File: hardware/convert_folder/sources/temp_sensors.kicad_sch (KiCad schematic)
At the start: 25 parts, among them CN14 TSW-101-05-T-S, IC6 MMBT3904, IC7 MMBT3904, U21 LTC2983CLX#PBF

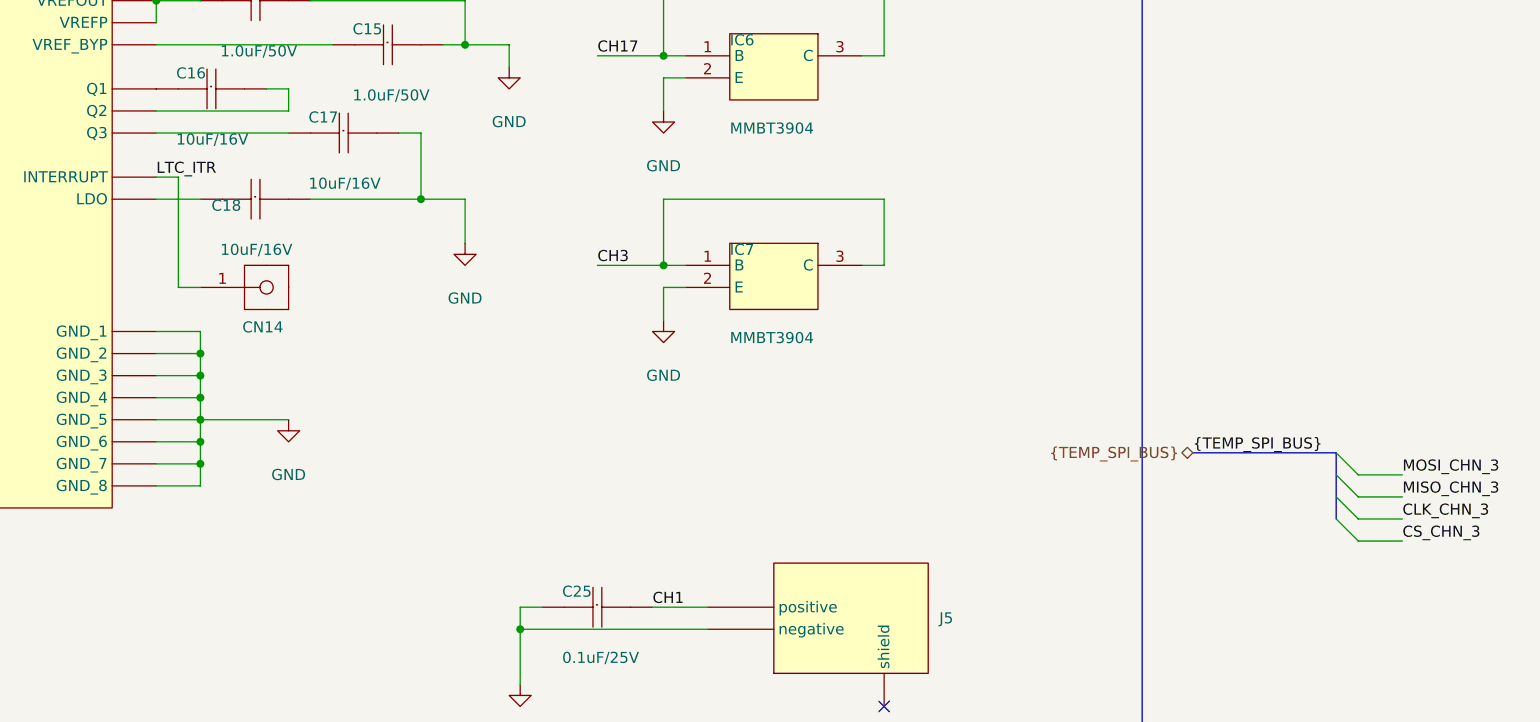
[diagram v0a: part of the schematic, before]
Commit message: fix: add more fixes to the power converters, add resets and other minor corrections
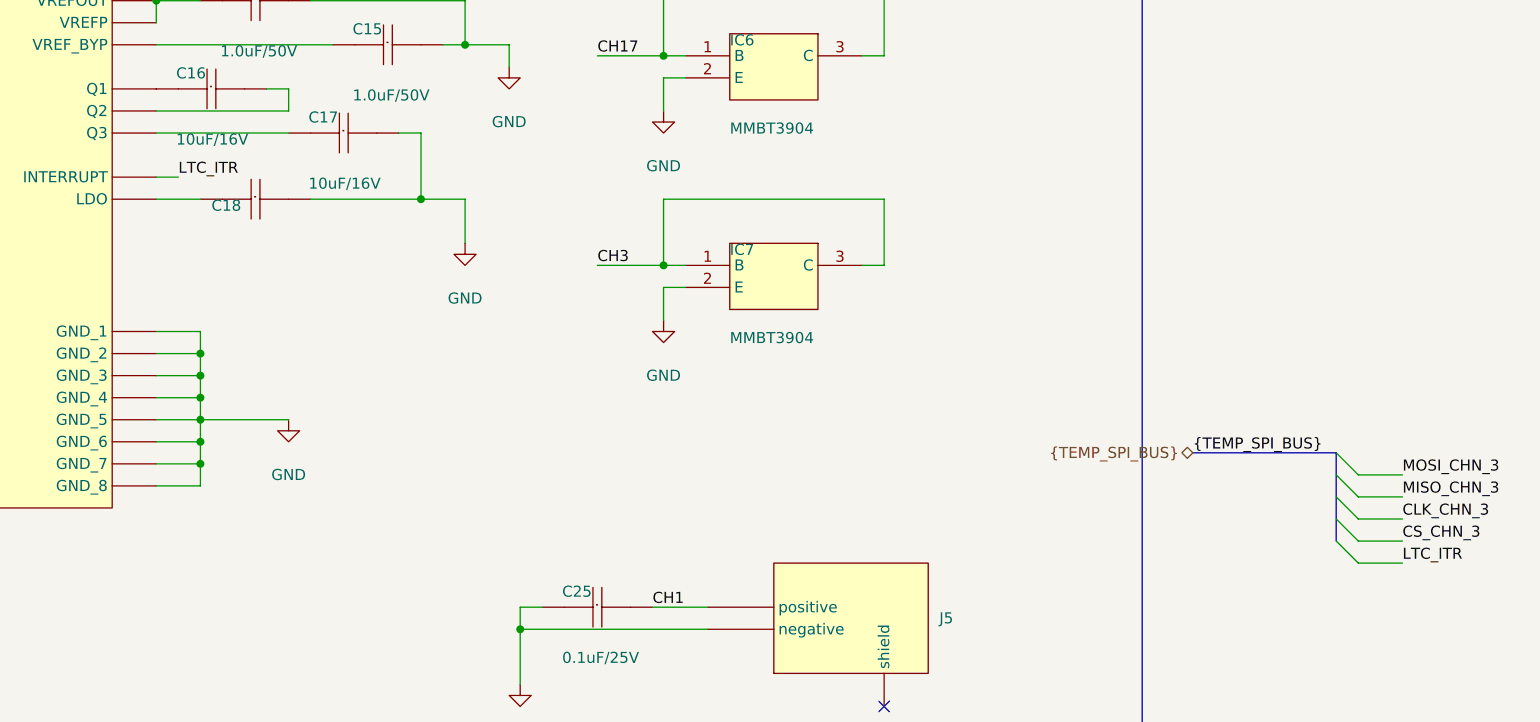
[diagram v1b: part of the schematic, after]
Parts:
- removed CN14: TSW-101-05-T-S, altium_import:PIN BAR 1 2.54mm 180 GRAUS - Hide, symbol altium_import:root_2_TSW-101-05-T-S_flatsat_platform_2.SchLib

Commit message: fix: finish regulators layout and fix many DRCs errors related to clearance
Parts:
- J10, J11, J12, J13, J14, J15, J5, J6: footprint altium_import:PCC-SMP-V-K -> lib:PCC-SMP-V-K-5
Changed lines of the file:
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@@
 	)
 	(symbol
-		(lib_name "root_0_PCC-SMP-V-K_Thermocouple_connector.SchLib_2")
 		(lib_id "altium_import:root_0_PCC-SMP-V-K_Thermocouple_connector.SchLib")
 		(at 289.56 255.27 90)
@@
 			)
 		)
-		(property "Footprint" "altium_import:PCC-SMP-V-K"
+		(property "Footprint" "lib:PCC-SMP-V-K-5"
 			(at 296.926 244.602 0)
 			(effects
@@
 	)
 	(symbol
-		(lib_name "root_0_PCC-SMP-V-K_Thermocouple_connector.SchLib_2")
 		(lib_id "altium_import:root_0_PCC-SMP-V-K_Thermocouple_connector.SchLib")
 		(at 290.83 278.13 90)
@@
 			)
 		)
-		(property "Footprint" "altium_import:PCC-SMP-V-K"
+		(property "Footprint" "lib:PCC-SMP-V-K-5"
 			(at 298.196 267.462 0)
 			(effects
@@
 	)
 	(symbol
-		(lib_name "root_0_PCC-SMP-V-K_Thermocouple_connector.SchLib_2")
 		(lib_id "altium_import:root_0_PCC-SMP-V-K_Thermocouple_connector.SchLib")
 		(at 346.71 278.13 90)
@@
 			)
 		)
-		(property "Footprint" "altium_import:PCC-SMP-V-K"
+		(property "Footprint" "lib:PCC-SMP-V-K-5"
 			(at 354.076 267.462 0)
 			(effects
@@
 	)
 	(symbol
-		(lib_name "root_0_PCC-SMP-V-K_Thermocouple_connector.SchLib_2")
 		(lib_id "altium_import:root_0_PCC-SMP-V-K_Thermocouple_connector.SchLib")
 		(at 232.41 254 90)
@@
 			)
 		)
-		(property "Footprint" "altium_import:PCC-SMP-V-K"
+		(property "Footprint" "lib:PCC-SMP-V-K-5"
 			(at 239.776 243.332 0)
 			(effects
@@
 	)
 	(symbol
-		(lib_name "root_0_PCC-SMP-V-K_Thermocouple_connector.SchLib_2")
 		(lib_id "altium_import:root_0_PCC-SMP-V-K_Thermocouple_connector.SchLib")
 		(at 233.68 278.13 90)
@@
 			)
 		)
-		(property "Footprint" "altium_import:PCC-SMP-V-K"
+		(property "Footprint" "lib:PCC-SMP-V-K-5"
 			(at 241.046 267.462 0)
 			(effects
@@
 	)
 	(symbol
-		(lib_name "root_0_PCC-SMP-V-K_Thermocouple_connector.SchLib_2")
 		(lib_id "altium_import:root_0_PCC-SMP-V-K_Thermocouple_connector.SchLib")
 		(at 345.44 229.87 90)
@@
 			)
 		)
-		(property "Footprint" "altium_import:PCC-SMP-V-K"
+		(property "Footprint" "lib:PCC-SMP-V-K-5"
 			(at 352.806 219.202 0)
 			(effects
@@
 	)
 	(symbol
-		(lib_name "root_0_PCC-SMP-V-K_Thermocouple_connector.SchLib_2")
 		(lib_id "altium_import:root_0_PCC-SMP-V-K_Thermocouple_connector.SchLib")
 		(at 346.71 255.27 90)
@@
 			)
 		)
-		(property "Footprint" "altium_import:PCC-SMP-V-K"
+		(property "Footprint" "lib:PCC-SMP-V-K-5"
 			(at 354.076 244.602 0)
 			(effects
@@
 	)
 	(symbol
-		(lib_name "root_0_PCC-SMP-V-K_Thermocouple_connector.SchLib_1")
 		(lib_id "altium_import:root_0_PCC-SMP-V-K_Thermocouple_connector.SchLib")
 		(at 346.71 203.2 90)
@@
 			)
 		)
-		(property "Footprint" "altium_import:PCC-SMP-V-K"
+		(property "Footprint" "lib:PCC-SMP-V-K-5"
 			(at 354.076 192.532 0)
 			(effects

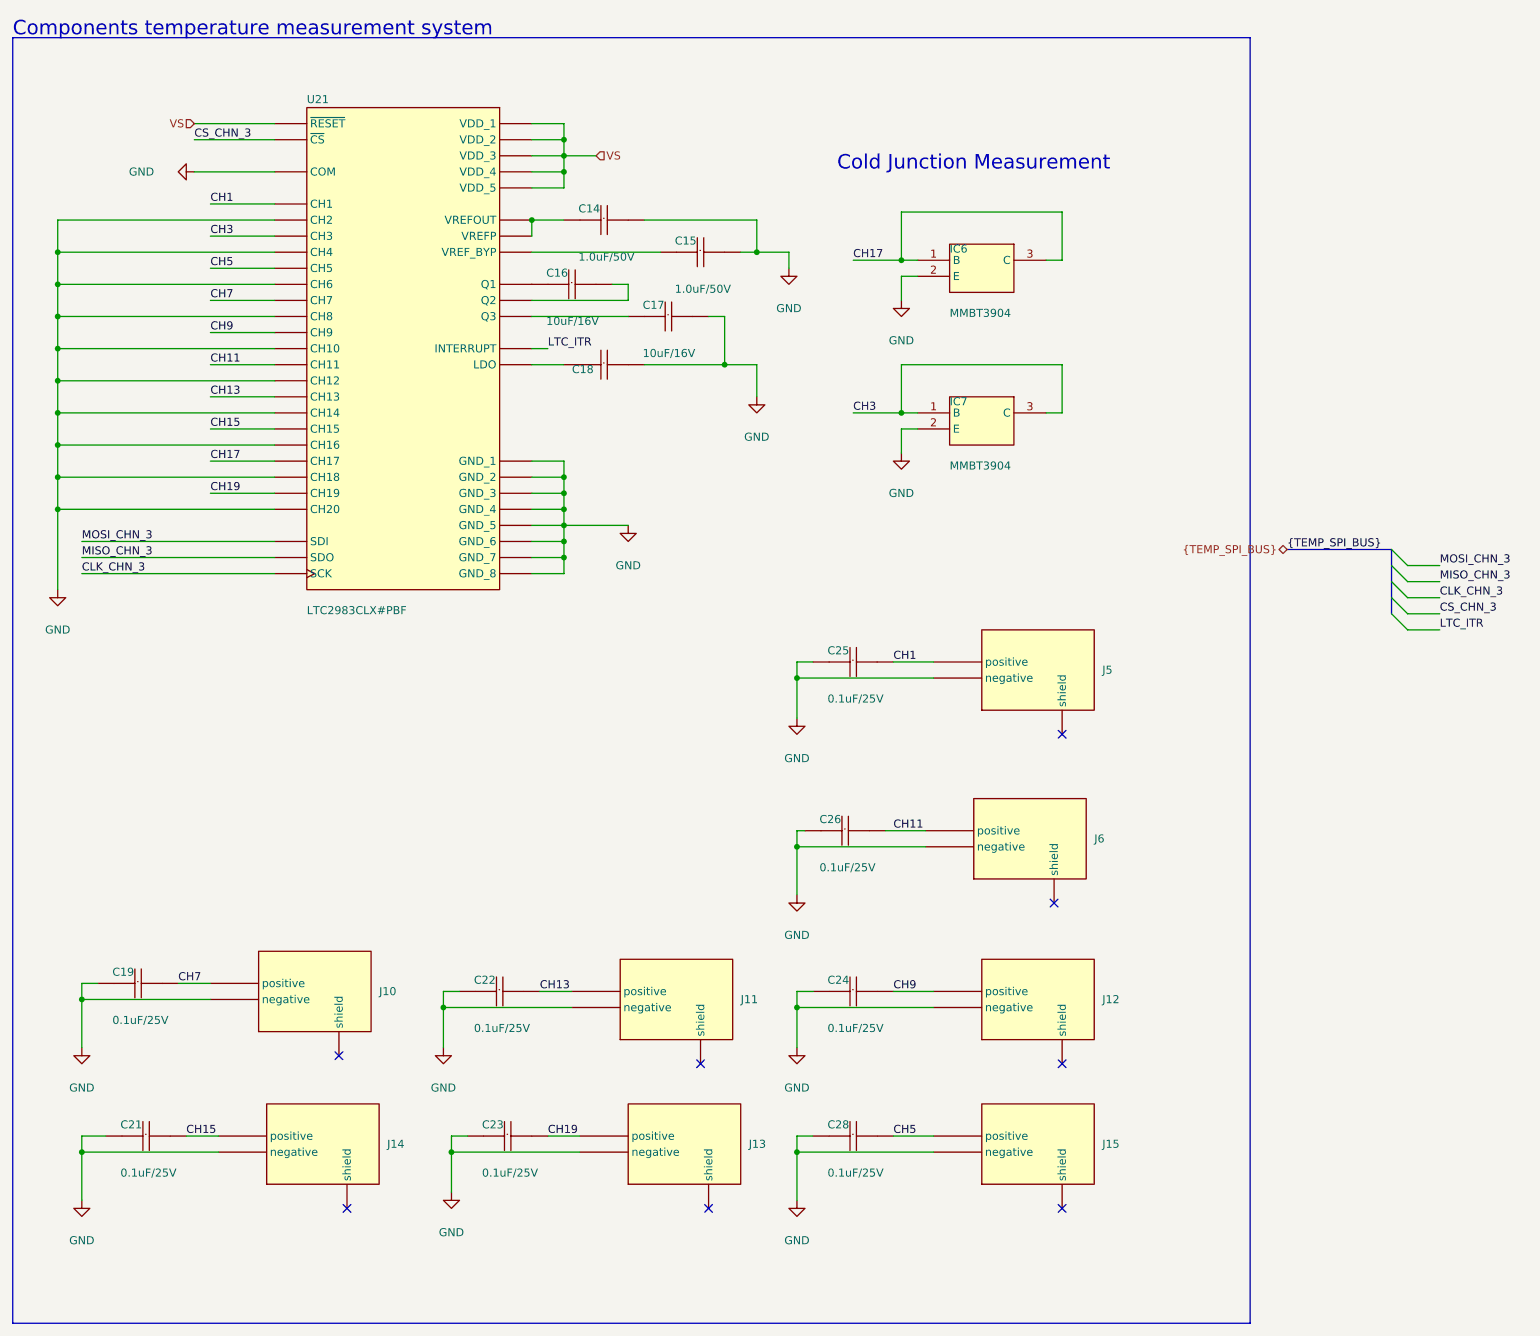
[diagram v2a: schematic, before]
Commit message: fix: improve LTC2983 circuit, fix some refs. positioning
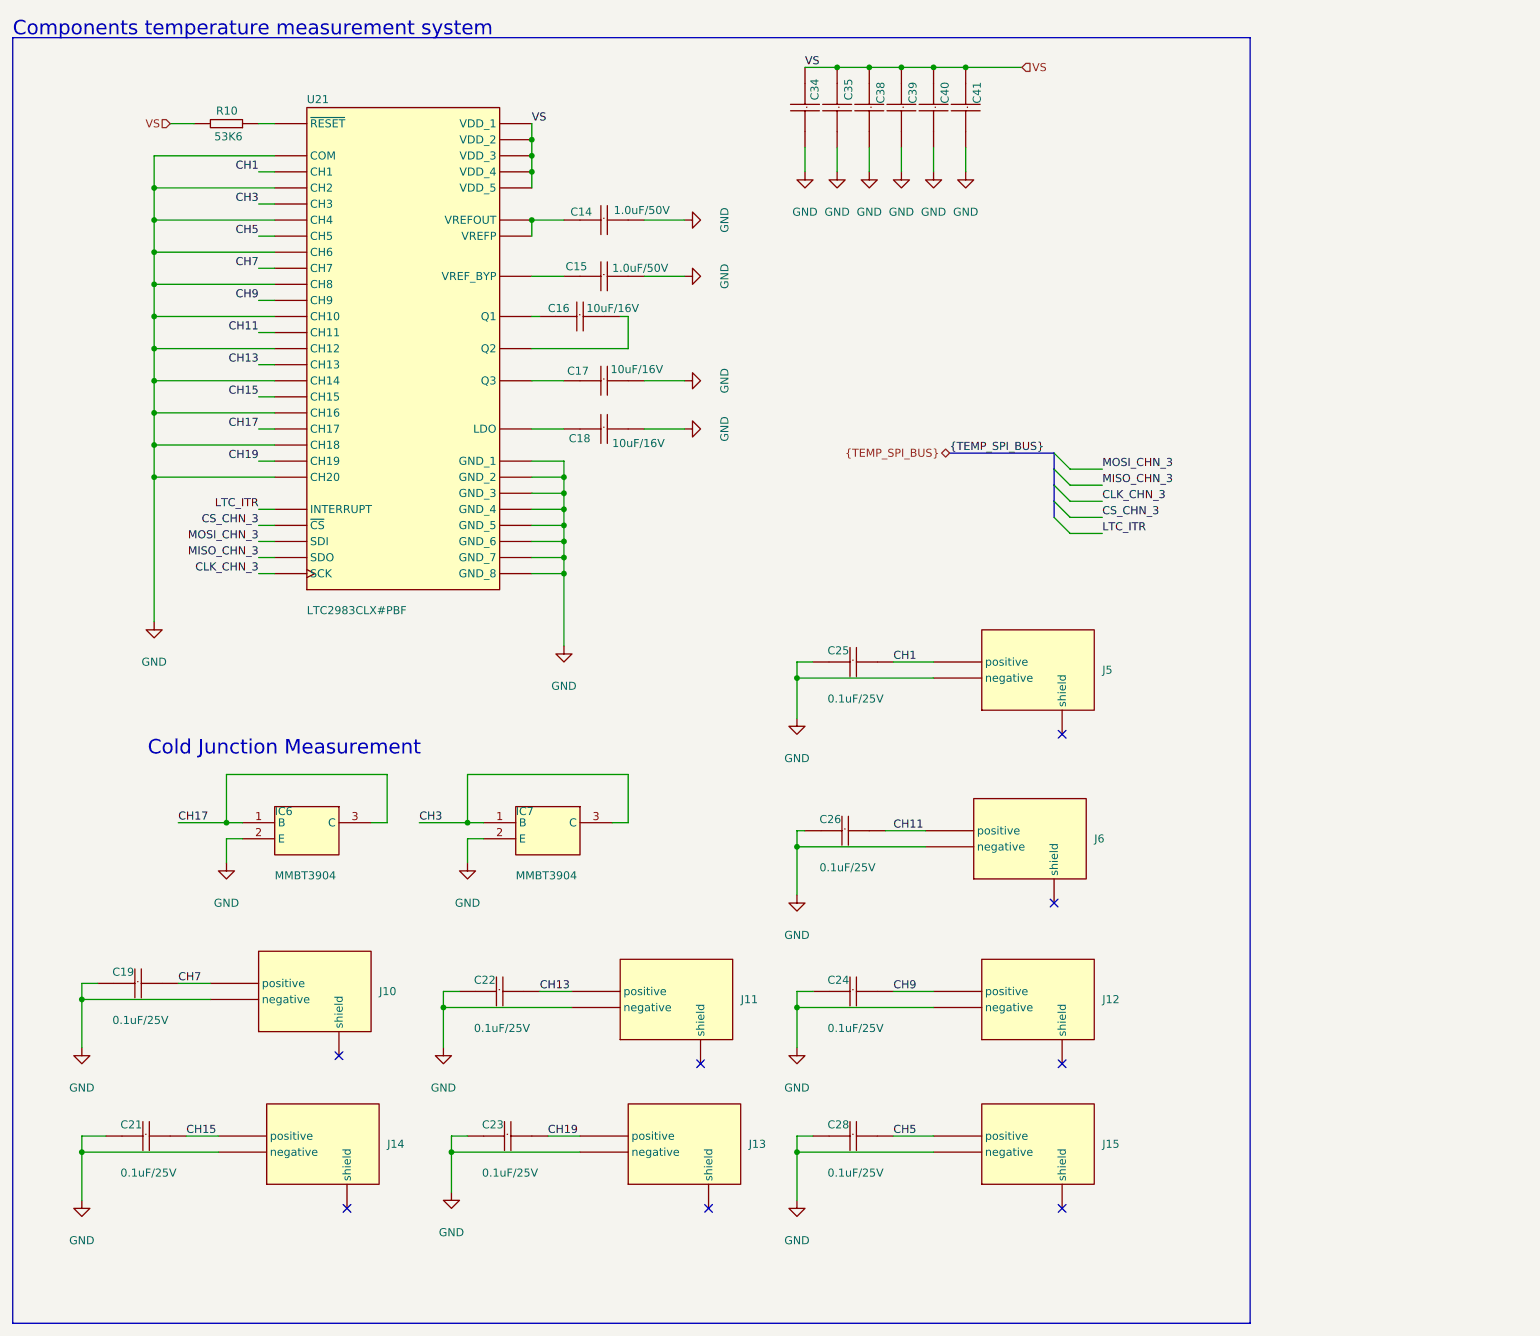
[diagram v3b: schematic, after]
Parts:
- added C34, C35: 10uF/16V, altium_import:CC1210, symbol altium_import:root_1_Cap_Cer_X7R_10uF_16V_1210_flatsat_platform_2.SchLib
- added C38, C39, C40, C41: 0.1uF/25V, altium_import:CC0805, symbol altium_import:root_1_Cap_Cer_X7R_0.1uF_25V_0805_flatsat_platform_2.SchLib
- added R10: ERJH3ED3652V, altium_import:R0603_HD, symbol altium_import:root_1_ERJH3ED3652V_SamacSys.SchLib
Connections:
- net GND: now also C34.2, C35.2, C38.2, C39.2, C40.2, C41.2
- net VS: now also C34.1, C35.1, C38.1, C39.1, C40.1, C41.1, R10.2; no longer U21.42 (~{RESET})
- new net: R10.1, U21.42 (~{RESET})
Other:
- moved on the sheet: C15, C16, C17, C18, IC6, IC7
